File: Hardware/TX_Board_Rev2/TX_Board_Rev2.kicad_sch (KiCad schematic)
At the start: 41 parts, among them IC1 GP2Y1+, IC2 GP2Y1+, IC24 ADP5600ACPZ-R7, IC25 TPS7A4701RGWT, IC27 ADPL40502AUJZ-1.8-R7, IC3 GP2Y1+, J1 Conn_Coaxial, J10 MM8030-2610RJ3, J11 MM8030-2610RJ3, J12 MM8030-2610RJ3, J19 694106301002, J20 Conn_01x08, J9 MM8030-2610RJ3, U1 SN74HCT138NSR

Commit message: Rev 2 progress
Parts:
- C134: footprint Capacitor_SMD:C_0603_1608Metric -> Capacitor_SMD:C_0402_1005Metric
- JP1, JP2: footprint Connector_PinHeader_2.54mm:PinHeader_1x11_P2.54mm_Vertical -> Connector_PinSocket_2.54mm:PinSocket_1x11_P2.54mm_Vertical
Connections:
- net ATTN_LE_4 is gone; now on net ATTN_LE_3: J20.1 (Pin_1), R5.2
- net PS_LE_4 is gone; now on net PS_LE_3: J20.5 (Pin_5), R9.2
- net ATTN_LE_0: now also J20.4 (Pin_4), R8.2
- net ATTN_LE_1: now also J20.3 (Pin_3), R7.2; no longer J20.4 (Pin_4), R8.2
- net ATTN_LE_2: now also J20.2 (Pin_2), R6.2; no longer J20.3 (Pin_3), R7.2
- net ATTN_LE_3: no longer J20.2 (Pin_2), R6.2
- net GND: now also JP1.3
- net PS_LE_0: now also J20.8 (Pin_8), R3.1
- net PS_LE_1: now also J20.7 (Pin_7), R11.2; no longer J20.8 (Pin_8), R3.1
- net PS_LE_2: now also J20.6 (Pin_6), R10.2; no longer J20.7 (Pin_7), R11.2
- net PS_LE_3: no longer J20.6 (Pin_6), R10.2
- no-connect marks 26 -> 25
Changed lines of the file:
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@@
 	)
 	(no_connect
-		(at 293.37 346.71)
-	)
-	(no_connect
 		(at 203.2 424.18)
 	)
@@
 		)
 	)
-	(global_label "PS_LE_1"
+	(global_label "PS_LE_0"
 		(shape input)
 		(at 53.34 267.97 180)
@@
 		)
 	)
-	(global_label "PS_LE_3"
+	(global_label "PS_LE_2"
 		(shape input)
 		(at 163.83 267.97 0)
@@
 		)
 	)
-	(global_label "ATTN_LE_3"
+	(global_label "ATTN_LE_2"
 		(shape input)
 		(at 163.83 257.81 0)
@@
 		)
 	)
-	(global_label "ATTN_LE_4"
+	(global_label "ATTN_LE_3"
 		(shape input)
 		(at 163.83 255.27 0)
@@
 		)
 	)
-	(global_label "PS_LE_2"
+	(global_label "PS_LE_1"
 		(shape input)
 		(at 163.83 270.51 0)
@@
 		)
 	)
-	(global_label "ATTN_LE_2"
+	(global_label "ATTN_LE_1"
 		(shape input)
 		(at 163.83 260.35 0)
@@
 		)
 	)
-	(global_label "PS_LE_4"
+	(global_label "PS_LE_3"
 		(shape input)
 		(at 163.83 265.43 0)
@@
 		)
 	)
-	(global_label "ATTN_LE_1"
+	(global_label "ATTN_LE_0"
 		(shape input)
 		(at 163.83 262.89 0)
@@
 			)
 		)
-		(property "Footprint" "Connector_PinHeader_2.54mm:PinHeader_1x11_P2.54mm_Vertical"
+		(property "Footprint" "Connector_PinSocket_2.54mm:PinSocket_1x11_P2.54mm_Vertical"
 			(at 295.91 354.33 0)
 			(effects
@@
 			)
 		)
-		(property "Footprint" "Capacitor_SMD:C_0603_1608Metric"
+		(property "Footprint" "Capacitor_SMD:C_0402_1005Metric"
 			(at 101.6 443.23 0)
 			(effects
@@
 	)
 	(symbol
+		(lib_id "power:GND")
+		(at 293.37 346.71 270)
+		(unit 1)
+		(exclude_from_sim no)
+		(in_bom yes)
+		(on_board yes)
+		(dnp no)
+		(fields_autoplaced yes)
+		(property "Reference" "#PWR0466"
+			(at 287.02 346.71 0)
+			(effects
+				(font
+					(size 1.27 1.27)
+				)
+				(hide yes)
+			)
+		)
+		(property "Value" "GND"
+			(at 289.56 346.7099 90)
+			(effects
+				(font
+					(size 1.27 1.27)
+				)
+				(justify right)
+			)
+		)
+		(property "Footprint" ""
+			(at 293.37 346.71 0)
+			(effects
+				(font
+					(size 1.27 1.27)
+				)
+				(hide yes)
+			)
+		)
+		(property "Datasheet" ""
+			(at 293.37 346.71 0)
+			(effects
+				(font
+					(size 1.27 1.27)
+				)
+				(hide yes)
+			)
+		)
+		(property "Description" "Power symbol creates a global label with name \"GND\" , ground"
+			(at 293.37 346.71 0)
+			(effects
+				(font
+					(size 1.27 1.27)
+				)
+				(hide yes)
+			)
+		)
+		(pin "1"
+		)
+		(instances
+			(project "TX_Board_Rev2"
+				(path "/5327d041-dca0-47c6-802d-ce81714adf6c"
+					(reference "#PWR0466")
+					(unit 1)
+				)
+			)
+		)
+	)
+	(symbol
 		(lib_id "tx_board_symbol_library:GND")
 		(at 190.5 190.5 180)
@@
 			)
 		)
-		(property "Footprint" "Connector_PinHeader_2.54mm:PinHeader_1x11_P2.54mm_Vertical"
+		(property "Footprint" "Connector_PinSocket_2.54mm:PinSocket_1x11_P2.54mm_Vertical"
 			(at 252.73 355.6 0)
 			(effects

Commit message: Rev2 Progress
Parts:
- removed J20: Conn_01x08, Connector_PinHeader_2.54mm:PinHeader_1x08_P2.54mm_Horizontal, symbol Connector_Generic:Conn_01x08
- added J18: Conn_01x08, Connector_PinHeader_2.54mm:PinHeader_1x08_P2.54mm_Vertical, symbol Connector_Generic:Conn_01x08
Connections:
- net ATTN_LE_0: now also R5.2; no longer R8.2
- net ATTN_LE_1: now also R6.2; no longer R7.2
- net ATTN_LE_2: now also R7.2; no longer R6.2
- net ATTN_LE_3: now also R8.2; no longer R5.2
- net CLK: now also J18.3 (Pin_3)
- net GND: now also J18.7 (Pin_7)
- net SER_IN: now also J18.4 (Pin_4)
- net SER_OUT: now also J18.5 (Pin_5)
- net TR_CTRL: now also J18.1 (Pin_1)
- net VCC: now also J18.8 (Pin_8)
- net VEE: now also J18.6 (Pin_6)
- net V_PD: now also J18.2 (Pin_2)

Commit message: Rev2 Complete
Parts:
- removed J1: Conn_Coaxial, Connector_Coaxial:SMA_Samtec_SMA-J-P-H-ST-EM1_EdgeMount, symbol tx_board_symbol_library:Conn_Coaxial
- added D1: LED, LED_SMD:LED_0805_2012Metric, symbol Device:LED
- added J20: CONSMA022-G, CONSMA022_G:LINX_CONSMA022-G, symbol CONSMA022-G:CONSMA022-G
- added R60: 100, Resistor_SMD:R_0402_1005Metric, symbol Device:R_US
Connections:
- net GND: now also J20.2, J20.3, J20.4, J20.5, R60.2
- net IC1-SUM_PORT: now also J20.1
- net DEVICE_ID: now reaches JP2.7
- net DEVICE_ID: now also D1.2 (A)
- new net: D1.1 (K), R60.1
- no-connect marks 25 -> 24

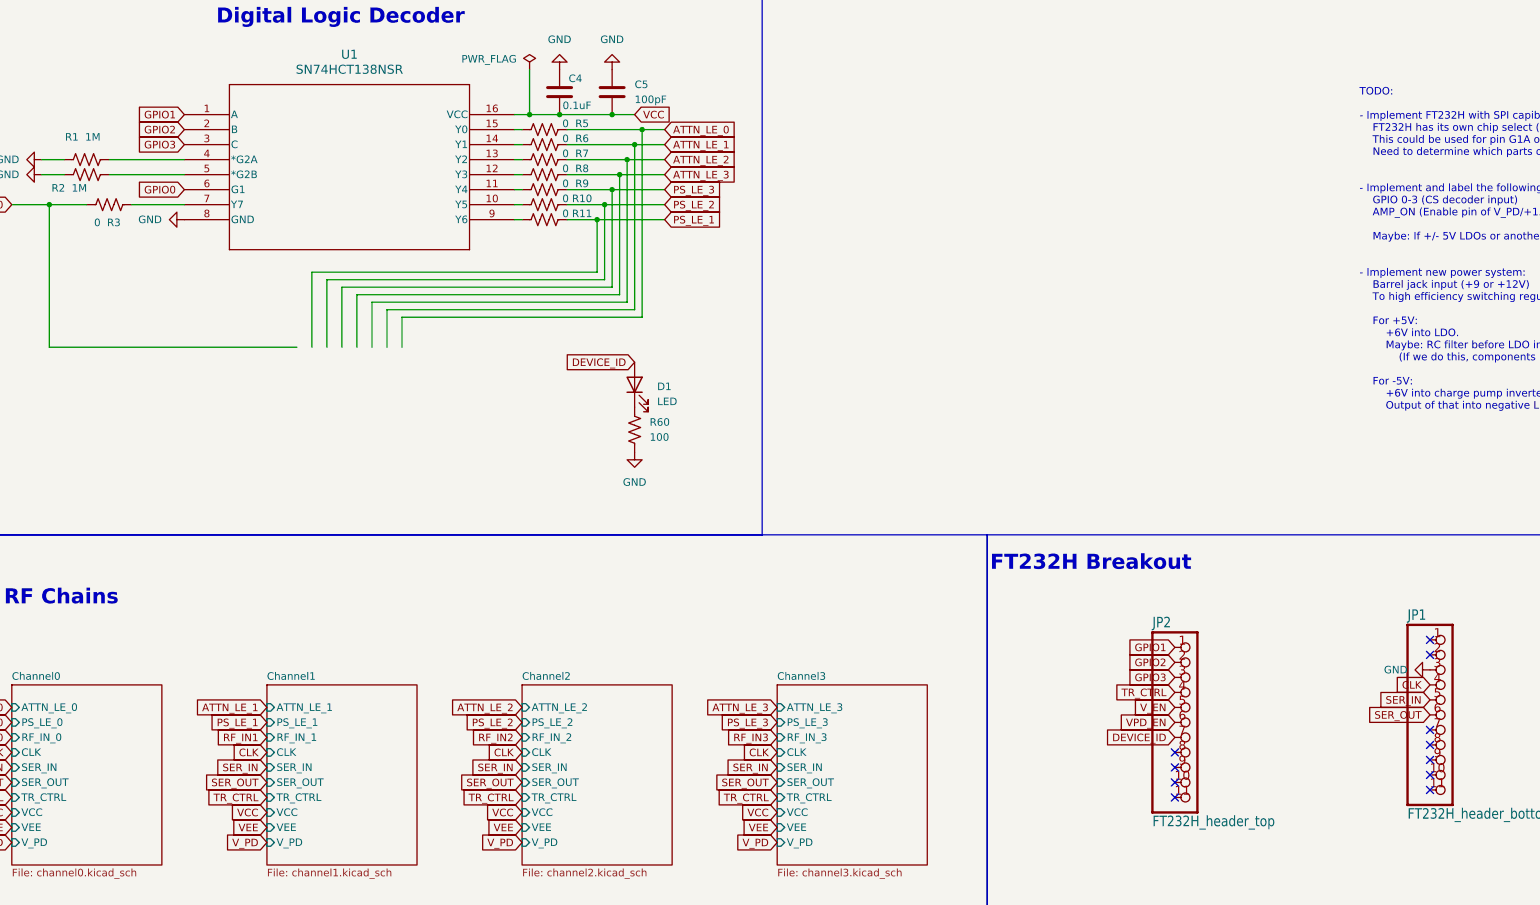
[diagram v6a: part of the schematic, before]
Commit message: FT232H Layout fix
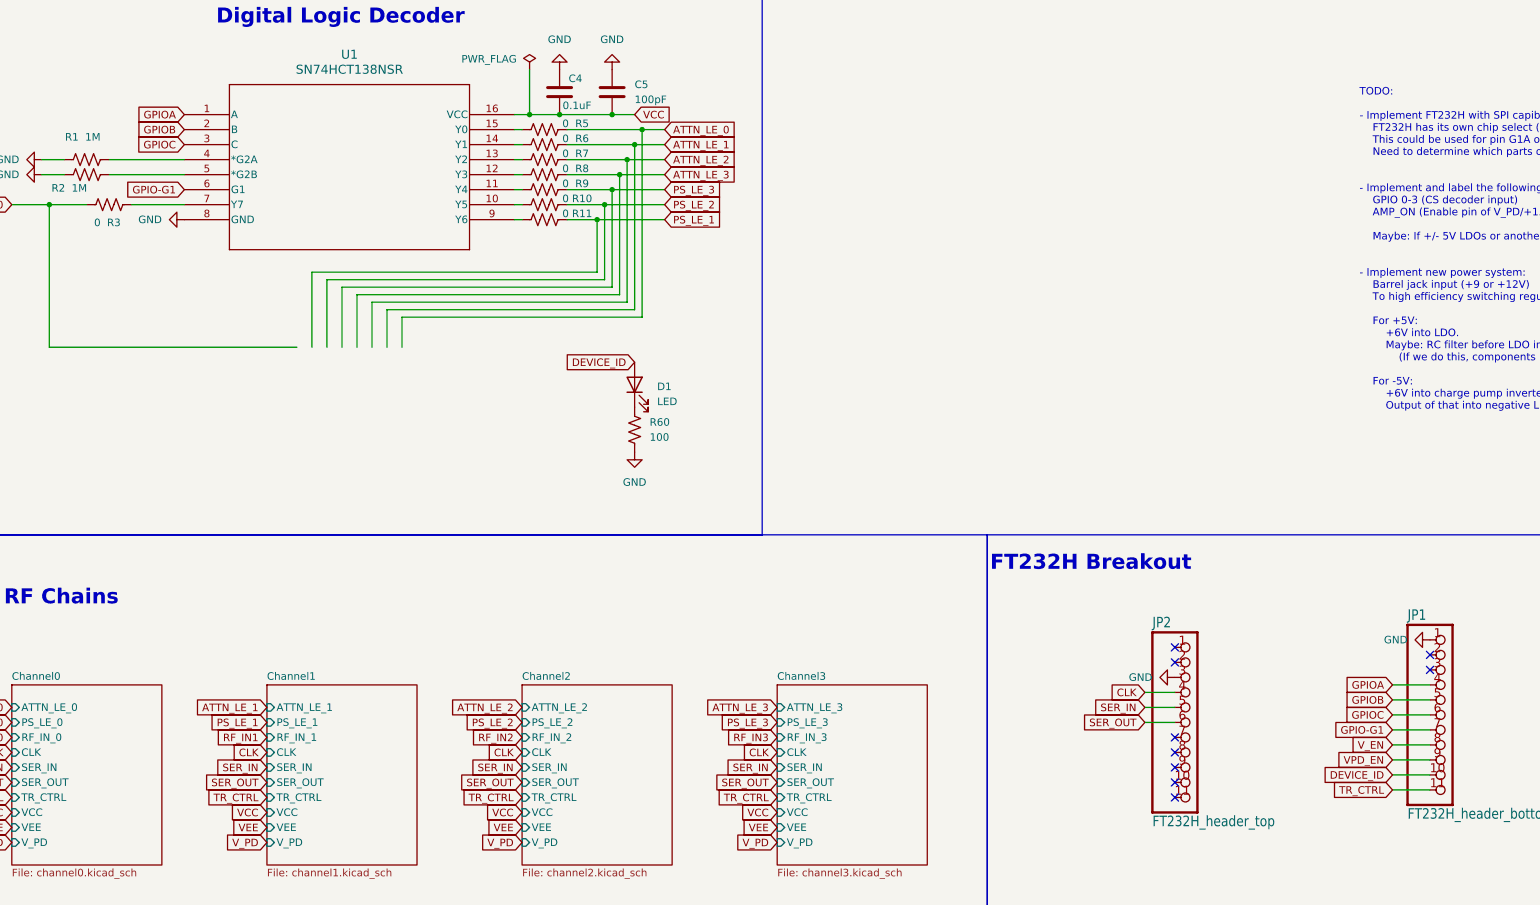
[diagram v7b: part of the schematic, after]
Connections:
- net GPIO0 is gone; now on net GPIO-G1: U1.6 (G1)
- net CLK: now also JP2.4; no longer JP1.4
- net DEVICE_ID: now also JP1.10; no longer JP2.7
- net GND: now also JP1.1, JP2.3; no longer JP1.3
- net SER_IN: now also JP2.5; no longer JP1.5
- net SER_OUT: now also JP2.6; no longer JP1.6
- net TR_CTRL: now also JP1.11; no longer JP2.4
- net VPD_EN: now also JP1.9; no longer JP2.6
- net V_EN: now also JP1.8; no longer JP2.5
- net GPIO-G1: now reaches JP1.7
- net GPIO1: no longer names the net of JP2.1
- net GPIO1: no longer U1.1 (A)
- net GPIO2: no longer names the net of JP2.2
- net GPIO2: no longer U1.2 (B)
- net GPIO3 renamed GPIOC
- net GPIOC: now also JP1.6; no longer JP2.3
- new net GPIOA: JP1.4, U1.1 (A)
- new net GPIOB: JP1.5, U1.2 (B)
- no-connect marks 24 -> 22

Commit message: Fix rev2
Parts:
- JP1, JP2: footprint Connector_PinSocket_2.54mm:PinSocket_1x11_P2.54mm_Vertical -> Connector_PinHeader_2.54mm:PinHeader_1x11_P2.54mm_Vertical
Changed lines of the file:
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@@
 			)
 		)
-		(property "Footprint" "Connector_PinSocket_2.54mm:PinSocket_1x11_P2.54mm_Vertical"
+		(property "Footprint" "Connector_PinHeader_2.54mm:PinHeader_1x11_P2.54mm_Vertical"
 			(at 295.91 354.33 0)
 			(effects
@@
 			)
 		)
-		(property "Footprint" "Connector_PinSocket_2.54mm:PinSocket_1x11_P2.54mm_Vertical"
+		(property "Footprint" "Connector_PinHeader_2.54mm:PinHeader_1x11_P2.54mm_Vertical"
 			(at 252.73 355.6 0)
 			(effects
